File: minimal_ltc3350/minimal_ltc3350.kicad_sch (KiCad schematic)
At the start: 20 parts, among them Q1 20.0 V, Q2 20.0 V, U1 LTC3350EUHF-PBF

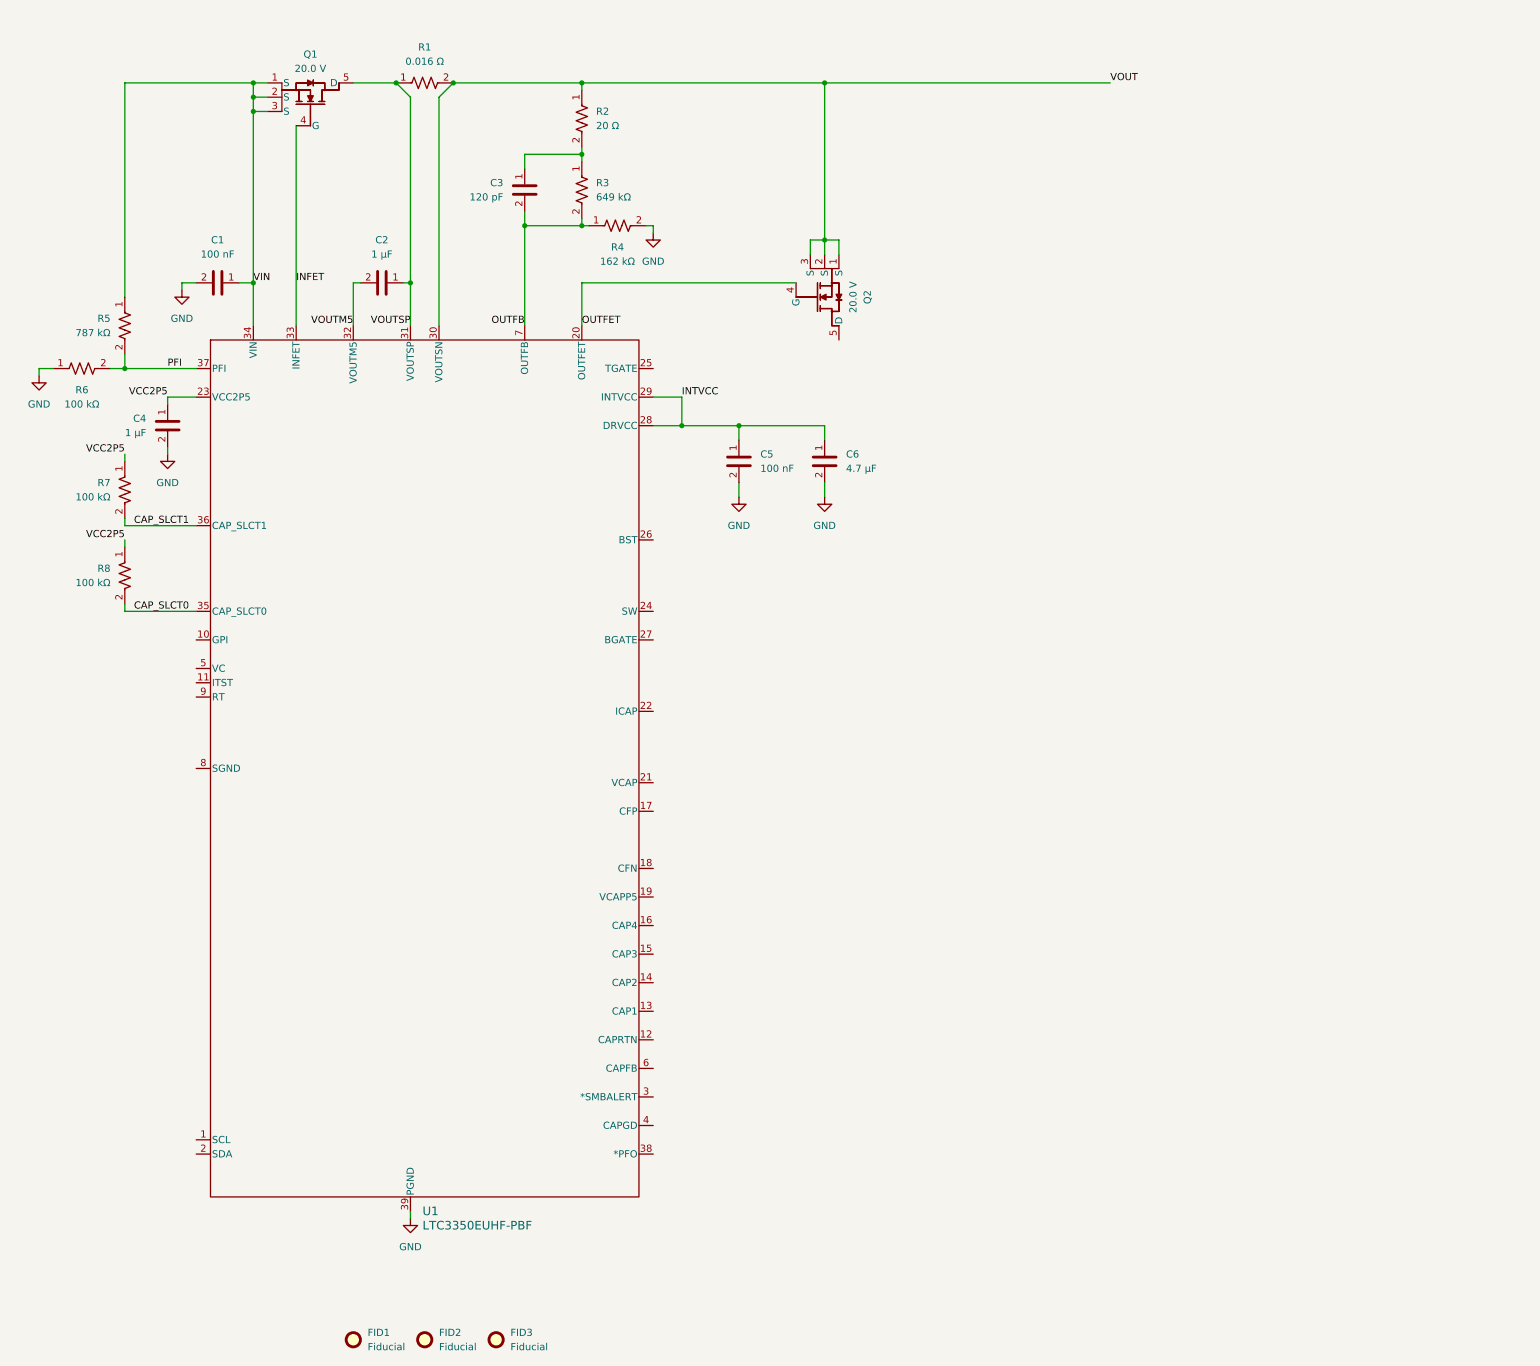
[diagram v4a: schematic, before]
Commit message: Update KiCad project: Component changes and layout improvements
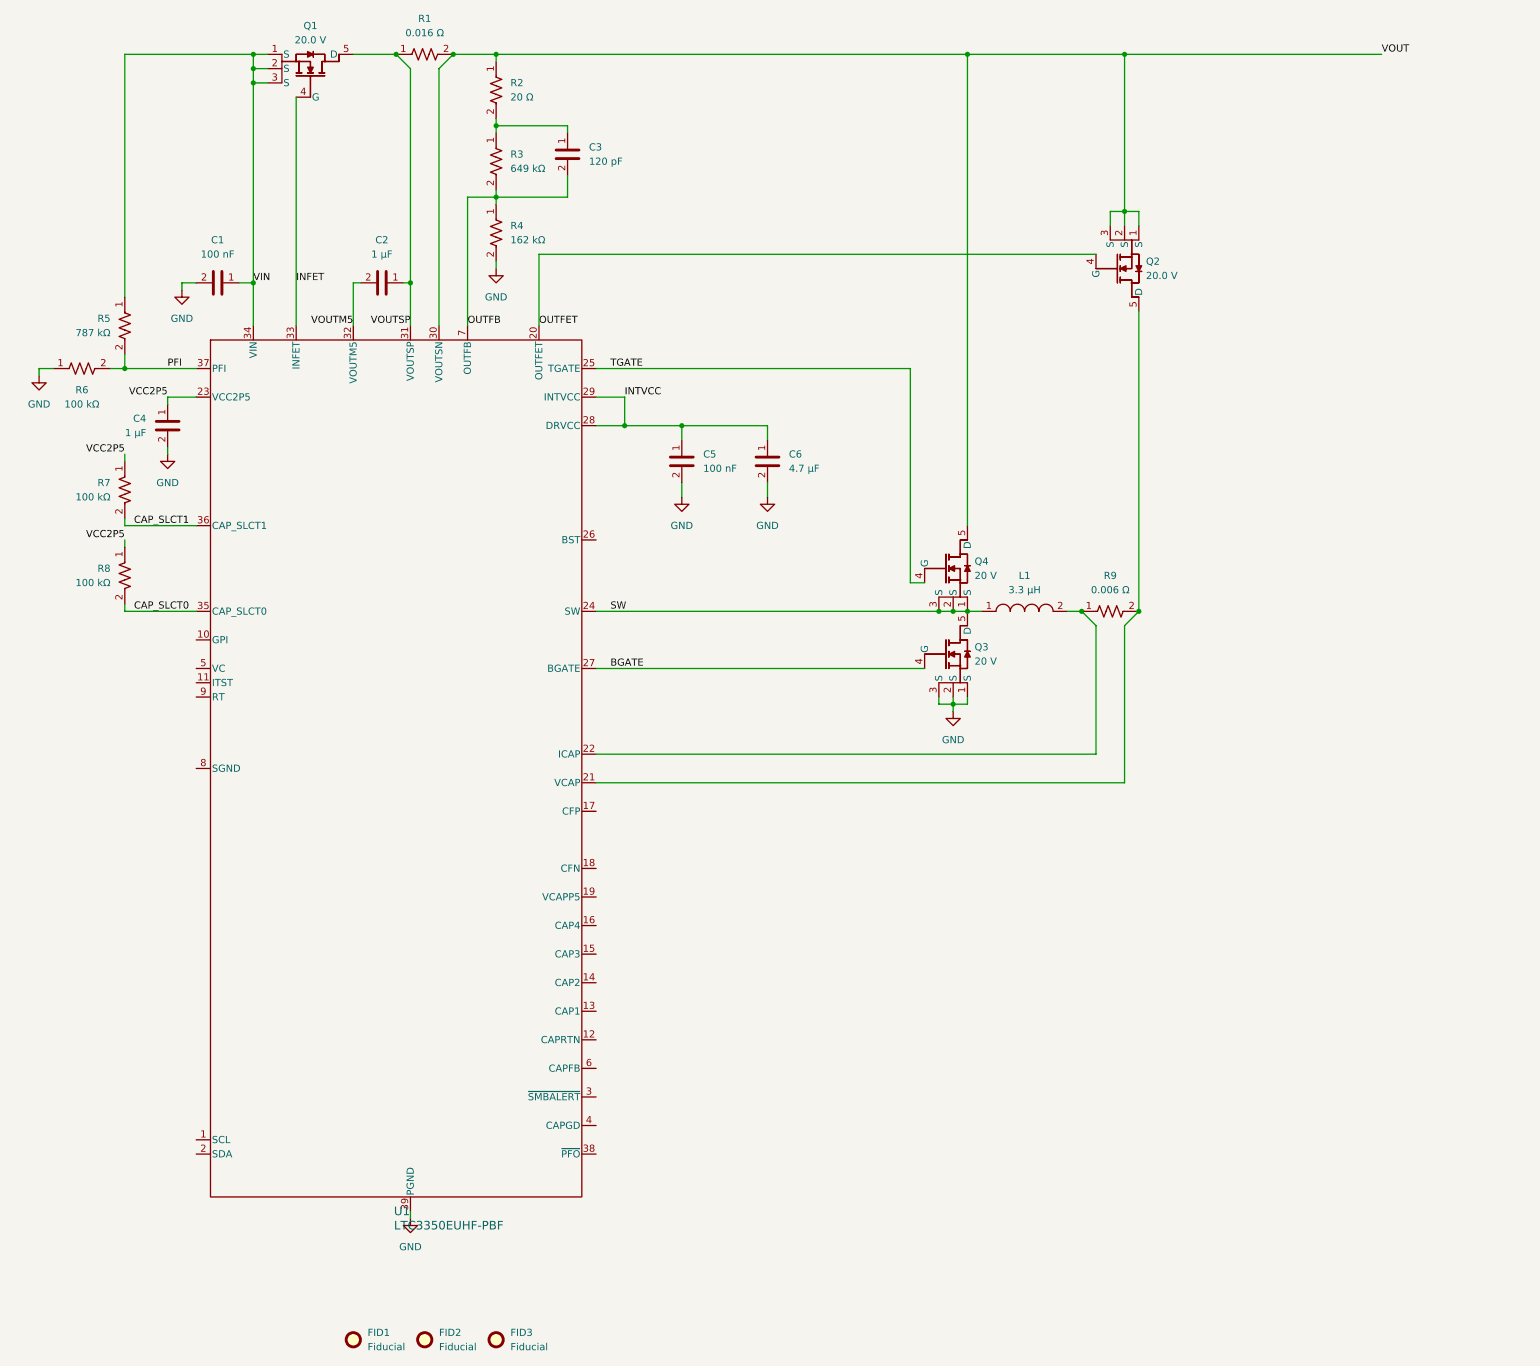
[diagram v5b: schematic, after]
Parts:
- added L1: 3.3 µH, inductor_footprints:XAL7030, symbol INDUCTORS_XAL7030_DATA_BASE:L_XAL7030-332ME
- added Q3, Q4: 20 V, transistor_footprints:TSDSON-8FL, symbol UNITED_TRANSISTORS_DATA_BASE:Q_BSZ060NE2LS
- added R9: 0.006 Ω, resistor_footprints:R_0612_1632Metric, symbol RESISTORS_PRL1632-_DATA_BASE:R_PRL1632-R006-F-T1
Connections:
- net GND: now also Q3.1 (S), Q3.2 (S), Q3.3 (S)
- net VOUT: now also Q4.5 (D)
- net at U1.21 (VCAP): now also Q2.5 (D), R9.2
- net at U1.22 (ICAP): now also L1.2, R9.1
- net SW: now reaches U1.24 (SW)
- net SW: now also L1.1, Q3.5 (D), Q4.1 (S), Q4.2 (S), Q4.3 (S)
- net TGATE: now reaches U1.25 (TGATE)
- net TGATE: now also Q4.4 (G)
- net BGATE: now reaches U1.27 (BGATE)
- net BGATE: now also Q3.4 (G)
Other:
- moved on the sheet: C3, C5, C6, Q1, Q2, R1, R2, R3, R4, U1

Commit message: Update KiCad project: Component changes, net updates, and symbol library additions
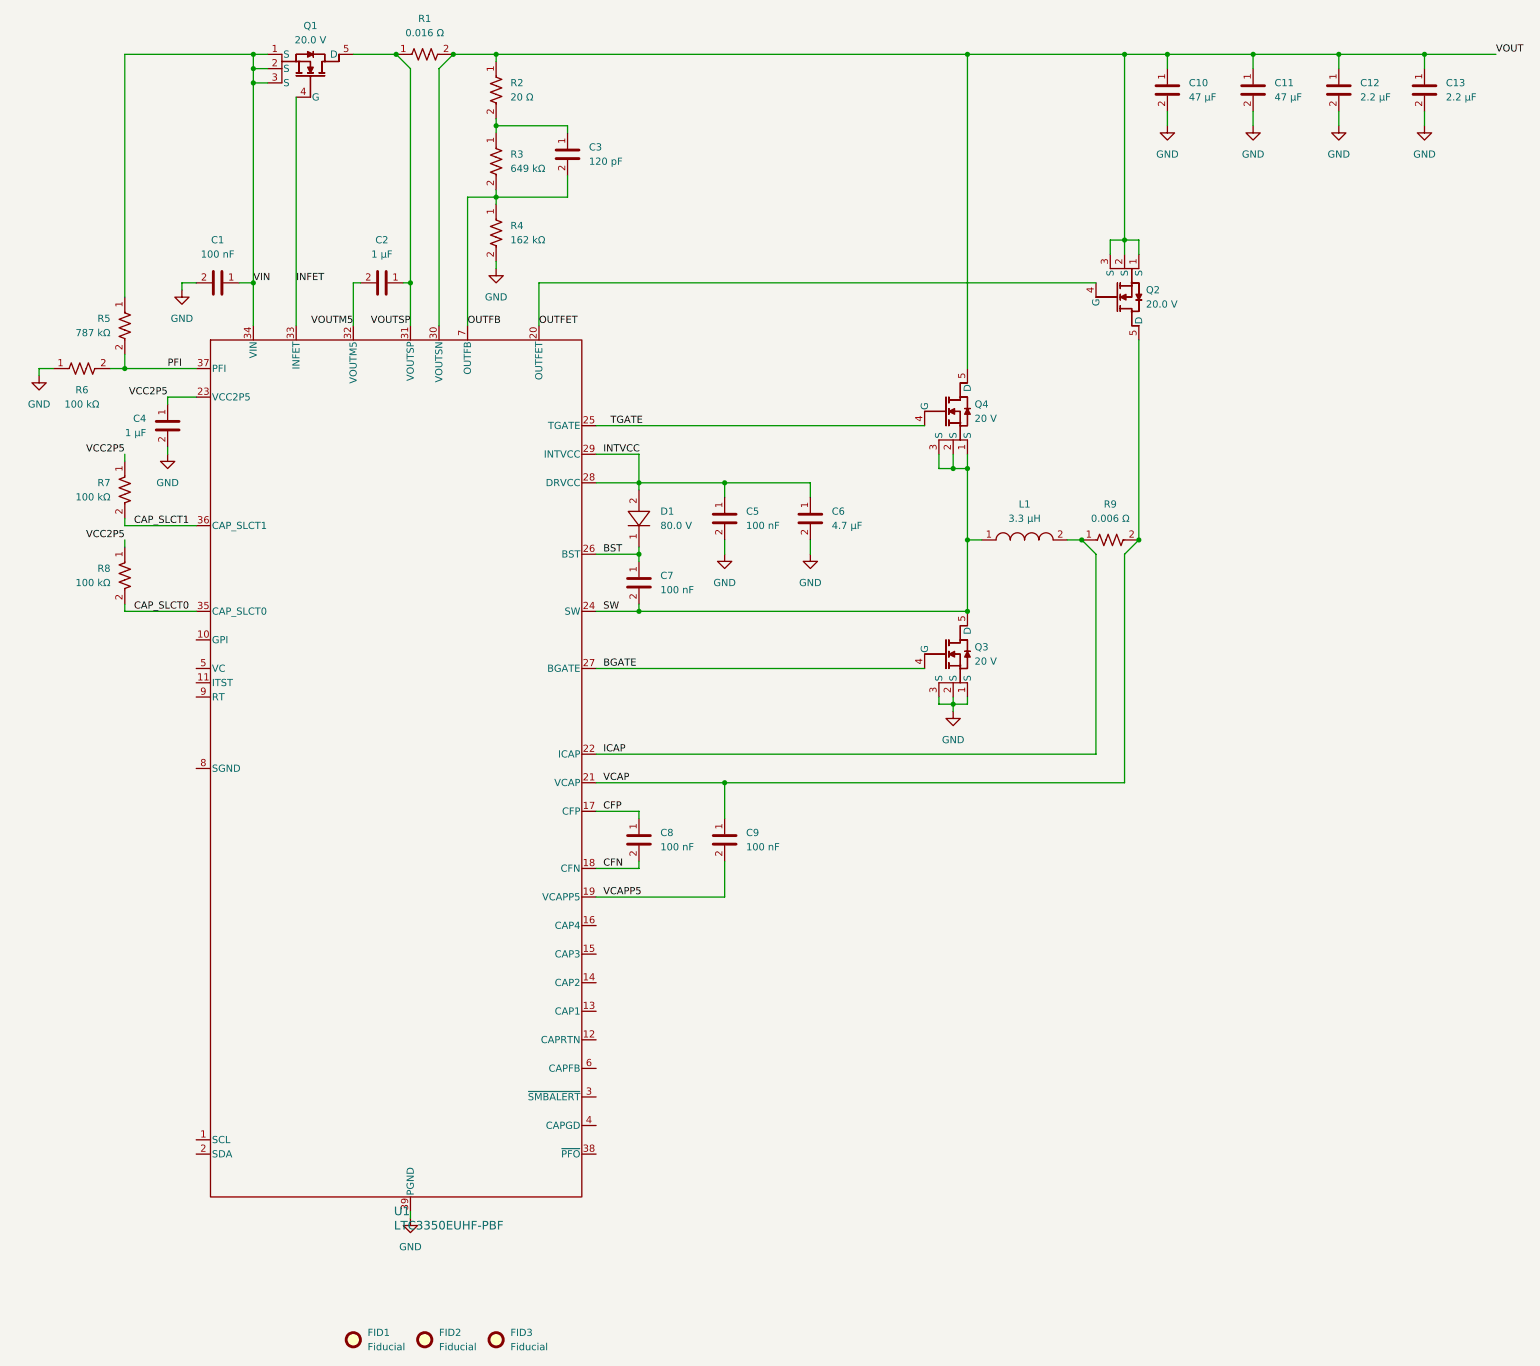
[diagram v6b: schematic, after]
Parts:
- added C10, C11: 47 µF, capacitor_footprints:C_1206_3216Metric, symbol CAPACITORS_C3216X5R1E_DATA_BASE:C_C3216X5R1E476M160AC
- added C12, C13: 2.2 µF, capacitor_footprints:C_0402_1005Metric, symbol CAPACITORS_C1005X5R1E_DATA_BASE:C_C1005X5R1E225K050BC
- added C7, C8, C9: 100 nF, capacitor_footprints:C_0402_1005Metric, symbol CAPACITORS_GCM155R71H_DATA_BASE:C_GCM155R71H104KE02D
- added D1: 80.0 V, diode_footprints:SOD_523, symbol DIODES_1N4448HWT-7_DATA_BASE:D_1N4448HWT-7
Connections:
- net GND: now also C10.2, C11.2, C12.2, C13.2
- net INTVCC: now also D1.2
- net SW: now also C7.2
- net VOUT: now also C10.1, C11.1, C12.1, C13.1
- net CFP: now reaches U1.17 (CFP)
- net CFP: now also C8.1
- net CFN: now reaches U1.18 (CFN)
- net CFN: now also C8.2
- net VCAPP5: now reaches U1.19 (VCAPP5)
- net VCAPP5: now also C9.2
- net VCAP: now reaches Q2.5 (D), R9.2, U1.21 (VCAP)
- net VCAP: now also C9.1
- net ICAP: now reaches L1.2, R9.1, U1.22 (ICAP)
- net BST: now reaches U1.26 (BST)
- net BST: now also C7.1, D1.1
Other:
- moved on the sheet: C5, C6, L1, Q2, Q4, R9

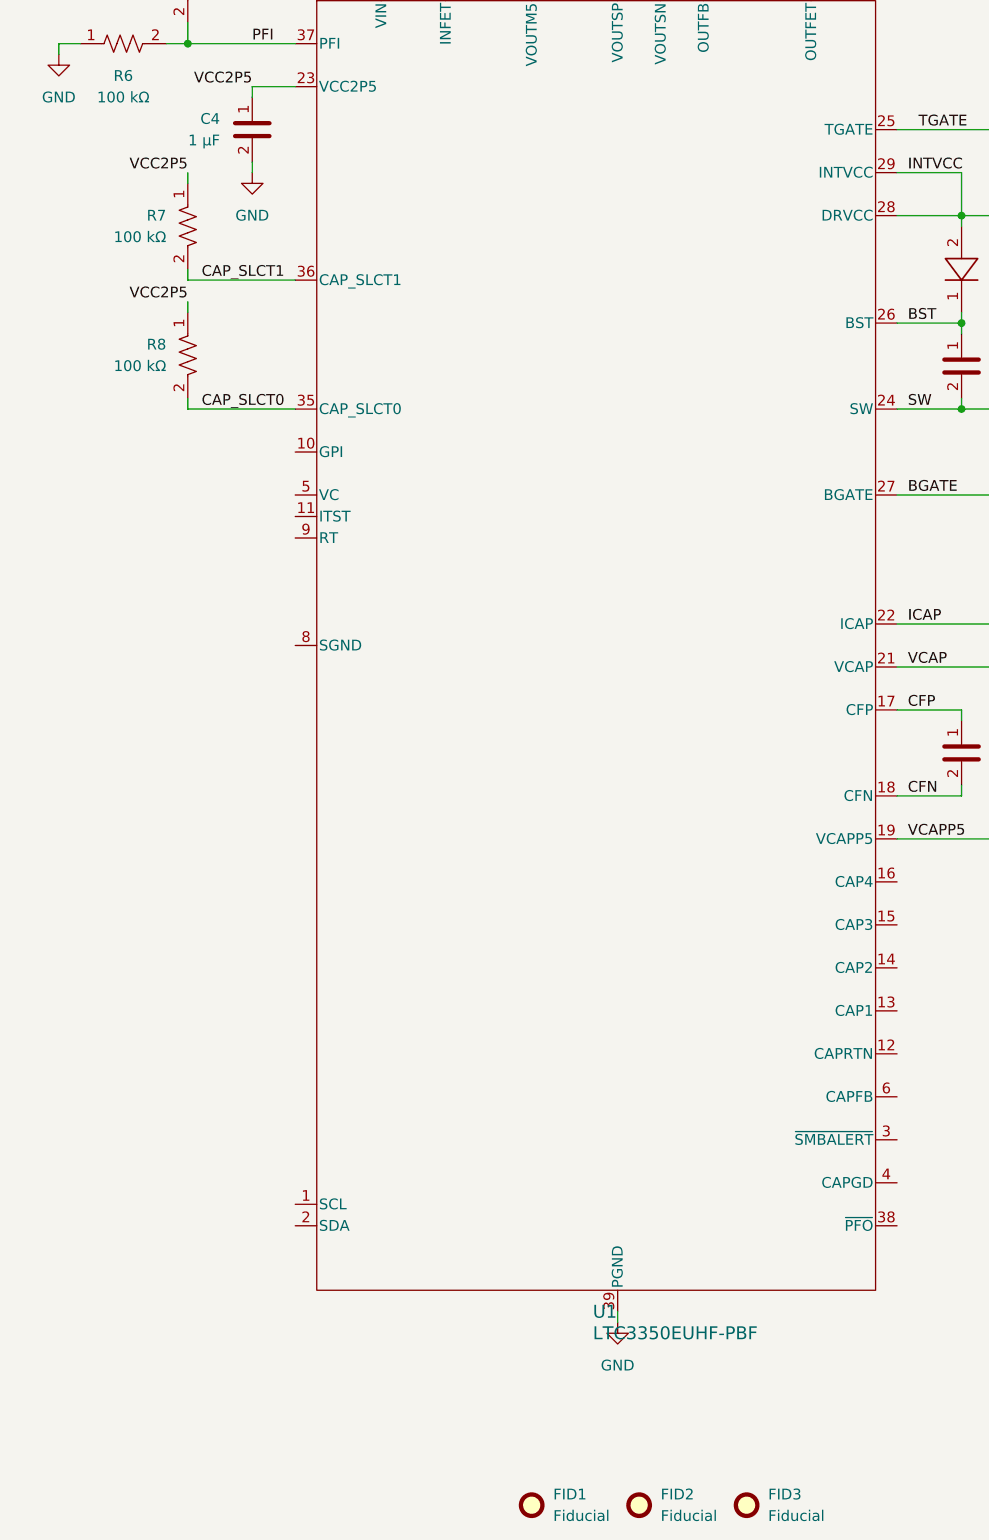
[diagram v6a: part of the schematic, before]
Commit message: Update KiCad project files: PCB layout, schematic, project settings, and symbols generator
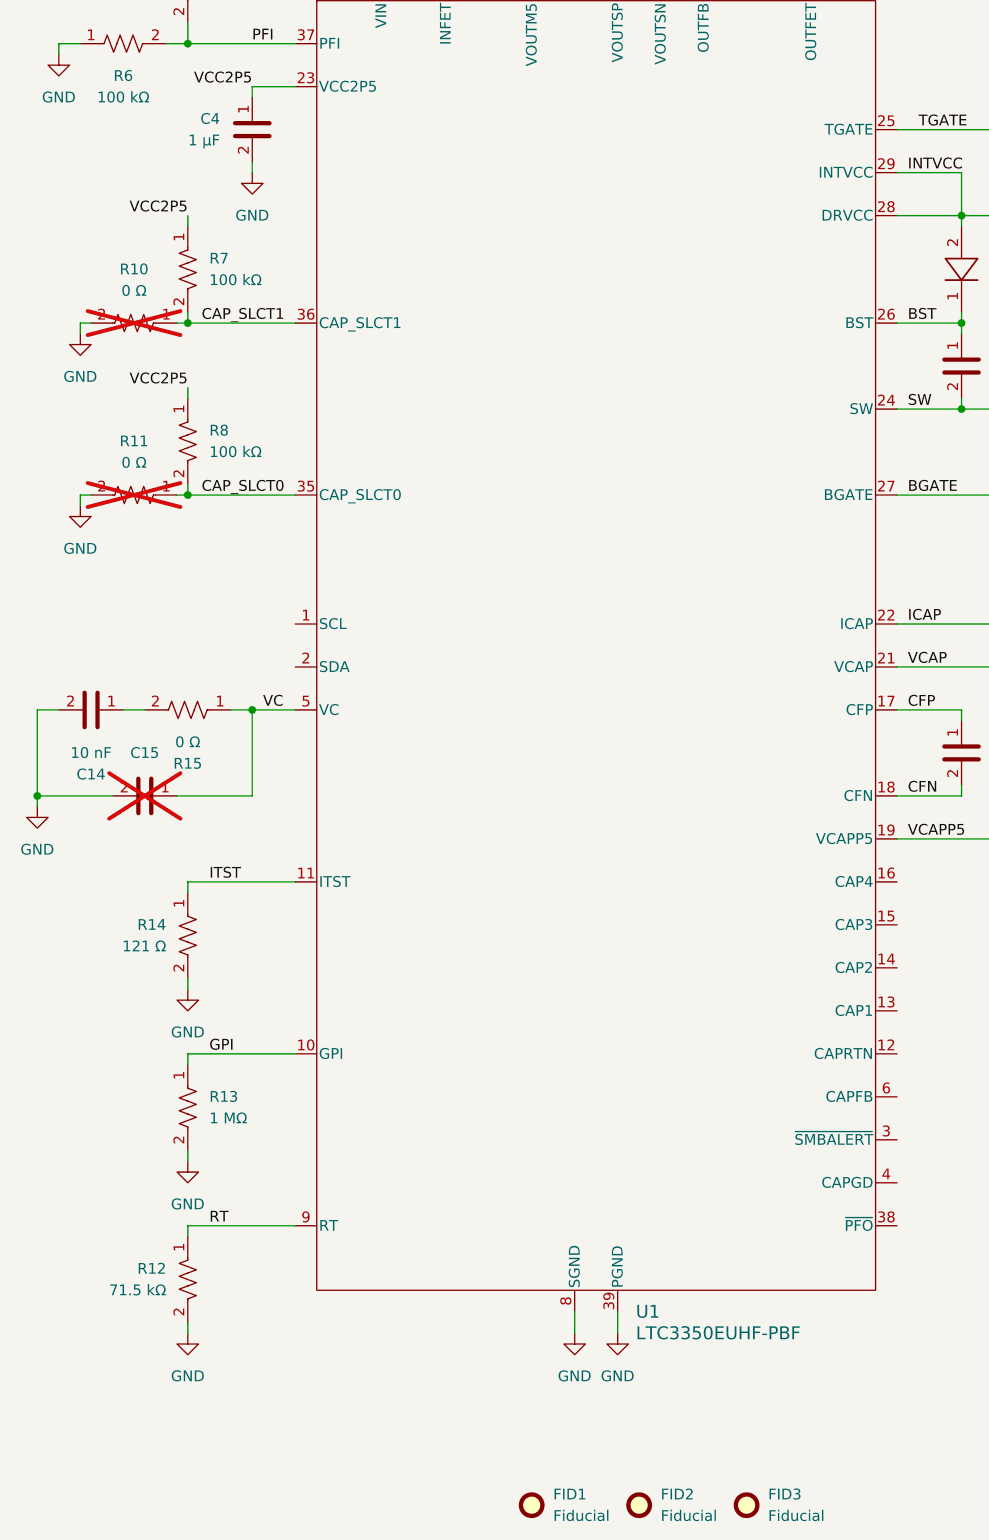
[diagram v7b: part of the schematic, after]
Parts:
- added C14, C15: 10 nF, capacitor_footprints:C_0402_1005Metric, symbol CAPACITORS_GCM155R71H_DATA_BASE:C_GCM155R71H103KA55D
- added R10, R11, R15: 0 Ω, resistor_footprints:R_0402_1005Metric, symbol RESISTORS_ERJ-2GE0_DATA_BASE:R_ERJ-2GE0R00X
- added R12: 71.5 kΩ, resistor_footprints:R_0402_1005Metric, symbol RESISTORS_ERJ-2RKF_DATA_BASE:R_ERJ-2RKF7152X
- added R13: 1 MΩ, resistor_footprints:R_0402_1005Metric, symbol RESISTORS_ERJ-2RKF_DATA_BASE:R_ERJ-2RKF1004X
- added R14: 121 Ω, resistor_footprints:R_0402_1005Metric, symbol RESISTORS_ERJ-2RKF_DATA_BASE:R_ERJ-2RKF1210X
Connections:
- net CAP_SLCT0: now also R11.1
- net CAP_SLCT1: now also R10.1
- net GND: now also U1.8 (SGND), C14.2, C15.2, R10.2, R11.2, R12.2, R13.2, R14.2
- net GPI: now reaches U1.10 (GPI)
- net GPI: now also R13.1
- net ITST: now reaches U1.11 (ITST)
- net ITST: now also R14.1
- net VC: now reaches U1.5 (VC)
- net VC: now also C15.1, R15.1
- net RT: now reaches U1.9 (RT)
- net RT: now also R12.1
- new net: C14.1, R15.2
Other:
- moved on the sheet: R7, R8

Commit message: Update KiCAD PCB and schematic files
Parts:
- added R16: 20 Ω, resistor_footprints:R_0402_1005Metric, symbol RESISTORS_ERJ-2RKF_DATA_BASE:R_ERJ-2RKF20R0X
- added R17: 866 kΩ, resistor_footprints:R_0402_1005Metric, symbol RESISTORS_ERJ-2RKF_DATA_BASE:R_ERJ-2RKF8663X
- added R18: 118 kΩ, resistor_footprints:R_0402_1005Metric, symbol RESISTORS_ERJ-2RKF_DATA_BASE:R_ERJ-2RKF1183X
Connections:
- net GND: now also R18.2
- net VCAP: now also R16.1
- net CAPFB: now reaches U1.6 (CAPFB)
- net CAPFB: now also R17.2, R18.1
- new net: R16.2, R17.1
